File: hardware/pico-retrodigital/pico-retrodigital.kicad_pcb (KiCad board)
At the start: 2 copper layers, 53.8 x 35 mm, 23 parts, among them J1 Conn_02x05_Top_Bottom, J2 HDMI_A, J3 Conn_01x04, J6 Conn_01x02_Pin, U1 SN74LVC8T245, U2 SN74LVC8T245, U3 SN74LVC8T245, U4 74LVC2G17, U6 SN74LVC126A, U7 RP2350B

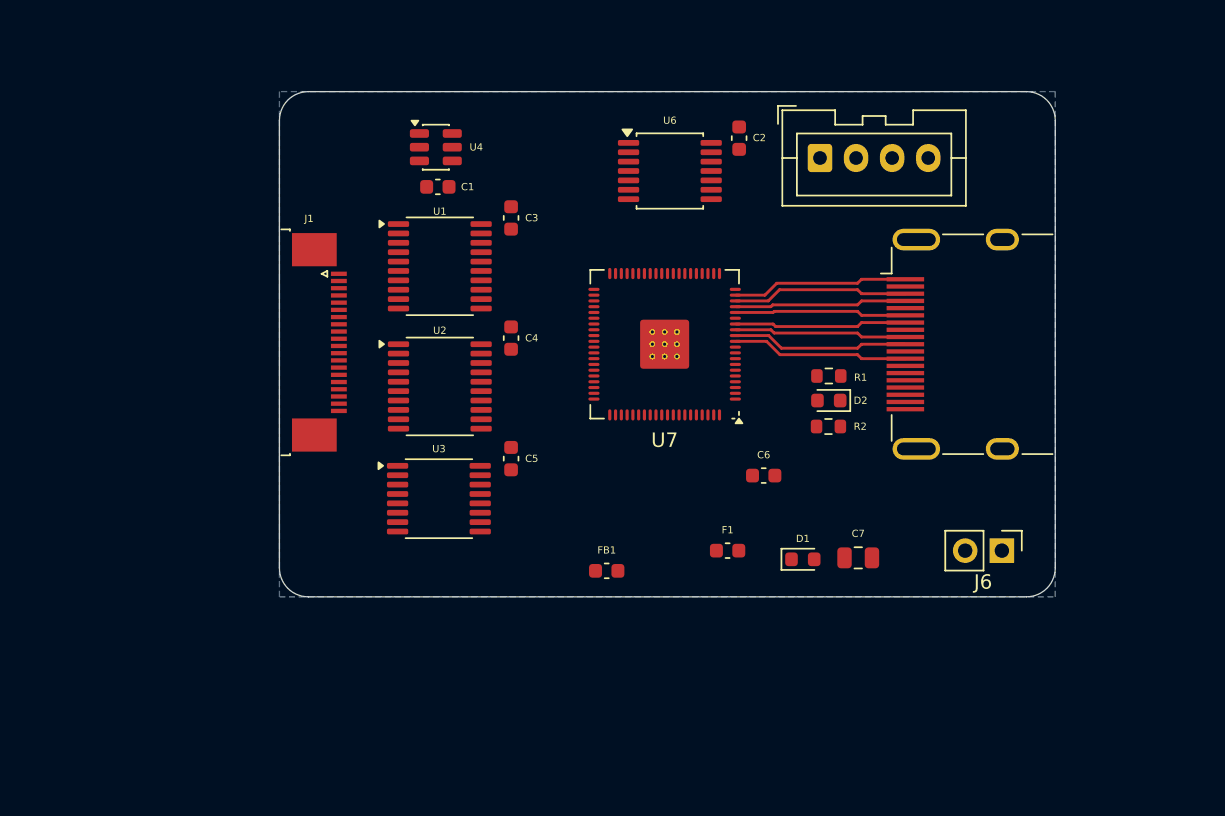
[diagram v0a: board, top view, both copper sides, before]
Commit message: Improve audio by adding 2s delay on startup
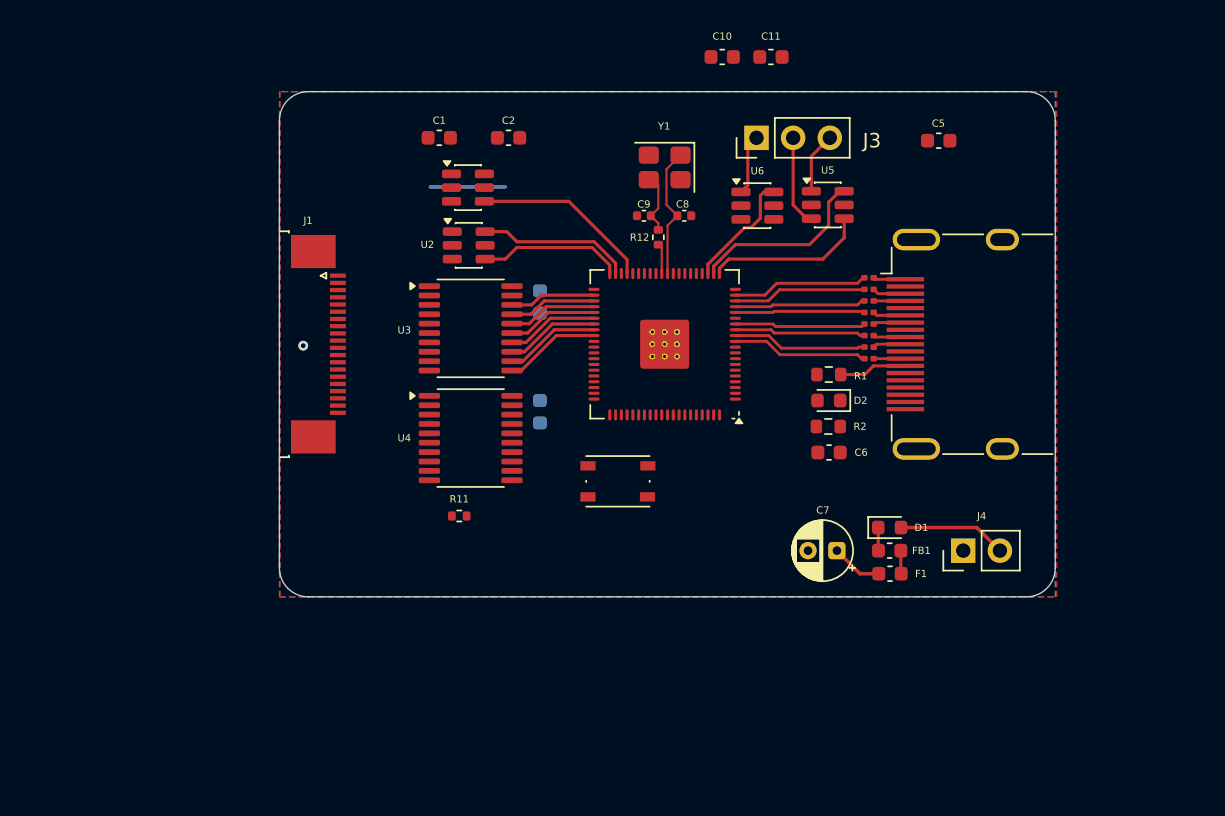
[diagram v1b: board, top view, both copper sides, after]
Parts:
- removed the C5 at (61.8, 100.4)
- removed J6: Conn_01x02_Pin, Connector_PinHeader_2.54mm:PinHeader_1x02_P2.54mm_Vertical
- removed the U3 at (56.8, 103.2)
- removed the U4 at (56.6, 78.8)
- added C10: 0.1u, Capacitor_SMD:C_0603_1608Metric, F.Cu at (76.4, 72.6)
- added C11: 0.1u, Capacitor_SMD:C_0603_1608Metric, F.Cu at (79.8, 72.6)
- added C2: 0.1u, Capacitor_SMD:C_0603_1608Metric, F.Cu at (61.6, 78.2)
- added C8: 15p, Capacitor_SMD:C_0402_1005Metric, F.Cu at (73.8, 83.6)
- added C9: 15p, Capacitor_SMD:C_0402_1005Metric, F.Cu at (71.0, 83.6)
- added J4: Conn_01x02_Pin, Connector_PinHeader_2.54mm:PinHeader_1x02_P2.54mm_Vertical, F.Cu at (93.1, 106.8)
- added R10: 220, Resistor_SMD:R_0201_0603Metric, F.Cu at (86.6, 87.9)
- added R11: 1k, Resistor_SMD:R_0402_1005Metric, F.Cu at (58.2, 104.4)
- added R12: 1k, Resistor_SMD:R_0402_1005Metric, F.Cu at (72.0, 85.1)
- added R3: 220, Resistor_SMD:R_0201_0603Metric, F.Cu at (86.6, 91.9)
- added R4: 220, Resistor_SMD:R_0201_0603Metric, F.Cu at (86.6, 93.5)
- added R5: 220, Resistor_SMD:R_0201_0603Metric, F.Cu at (86.6, 92.7)
- added R6: 220, Resistor_SMD:R_0201_0603Metric, F.Cu at (86.6, 91.1)
- added R7: 220, Resistor_SMD:R_0201_0603Metric, F.Cu at (86.6, 90.3)
- added R8: 220, Resistor_SMD:R_0201_0603Metric, F.Cu at (86.6, 89.5)
- added R9: 220, Resistor_SMD:R_0201_0603Metric, F.Cu at (86.6, 88.7)
- added SW1: SW_Push, Button_Switch_SMD:SW_Push_1P1T_NO_Vertical_Wuerth_434133025816, F.Cu at (69.2, 102.0)
- added U1: 74LVC2G17, Package_TO_SOT_SMD:SOT-23-6, F.Cu at (58.8, 81.7)
- added U2: 74LVC2G17, Package_TO_SOT_SMD:SOT-23-6, F.Cu at (58.9, 85.7)
- added U5: 74LVC2G17, Package_TO_SOT_SMD:SOT-23-6, F.Cu at (83.7, 82.8)
- added Y1: ABM8-272-T3, Crystal:Crystal_SMD_3225-4Pin_3.2x2.5mm, F.Cu at (72.4, 80.2)
- C3, C4: moved to B.Cu
- C7: footprint Capacitor_SMD:C_0805_2012Metric -> Capacitor_THT:CP_Radial_D4.0mm_P2.00mm
- J3: value Conn_01x04 -> Conn_01x03; footprint Connector_JST:JST_XA_B04B-XASK-1_1x04_P2.50mm_Vertical -> Connector_PinHeader_2.54mm:PinHeader_1x03_P2.54mm_Vertical
- U6: value SN74LVC126A -> 74LVC2G17; footprint Package_SO:TSSOP-14_4.4x5mm_P0.65mm -> Package_TO_SOT_SMD:SOT-23-6
- moved FB1 19.6 mm to (88.0, 106.8)
- moved C5 13.8 mm to (91.4, 78.4), turned to 0 degrees
- moved F1 11.4 mm to (88.0, 108.4), turned to 180 degrees
- moved U6 6.52 mm to (78.9, 82.9)
- moved D1 6.40 mm to (88.0, 105.2)
- moved C3 6.16 mm to (63.8, 89.6)
- moved C4 5.48 mm to (63.8, 97.2)
- moved U3 4.80 mm to (59.0, 91.4)
- moved C6 4.80 mm to (83.8, 100.0)
- moved J3 4.62 mm to (78.8, 78.2), turned to 90 degrees
- moved U4 4.17 mm to (59.0, 99.0)
- moved C1 3.40 mm to (56.8, 78.2), turned to 0 degrees
- moved C7 1.56 mm to (84.4, 106.8), turned to 180 degrees
- moved J1 0.15 mm to (48.5, 92.5)
- moved R1 0.10 mm to (83.8, 94.6)
- renumbered C2 to C5, U1 to U3, U2 to U4
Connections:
- C1 pad 1: +3V3 -> 3V3
- C3 pad 1: +3.3V -> 3V3
- C4 pad 1: +3.3V -> 3V3
- C7 pad 1: +5V -> 5V
- D1 pad 2: +5V MVS -> 5V
- D2 pad 2: +5V -> 5V
- F1 pad 2: +5V -> 5V
- J1 pad 1: IN_PCLK -> IN_VID_S
- J1 pad 10: IN_G1 -> IN_R4
- J1 pad 11: IN_G2 -> IN_G0
- J1 pad 12: IN_G3 -> IN_G1
- J1 pad 13: IN_G4 -> IN_G2
- J1 pad 14: IN_B0 -> IN_G3
- J1 pad 15: IN_B1 -> IN_G4
- J1 pad 16: IN_B2 -> IN_B0
- J1 pad 17: IN_B3 -> IN_B1
- J1 pad 18: IN_B4 -> IN_B2
- J1 pad 19: IN_VID_A -> IN_B3
- J1 pad 2: GND -> IN_PCLK
- J1 pad 20: IN_VID_B -> IN_B4
- J1 pad 3: IN_VID_C -> GND
- J1 pad 4: IN_R0 -> IN_VID_D1
- J1 pad 5: IN_R1 -> IN_VID_D2
- J1 pad 6: IN_R2 -> IN_R0
- J1 pad 7: IN_R3 -> IN_R1
- J1 pad 8: IN_R4 -> IN_R2
- J1 pad 9: IN_G0 -> IN_R3
- J3 pad 2: GND -> IN_AUD_B
- J3 pad 3: IN_AUD_B -> IN_AUD_A
- R1 pad 1: +3V3 -> 3V3
- R2 pad 1: +5V -> 5V
- U3 pad 20: +3.3V -> 3V3
- U4 pad 20: +3.3V -> 3V3
- U6 pad 1: unconnected-(U6-~{1OE}-Pad1) -> IN_AUD_C
- U6 pad 2: IN_AUD_A -> GND
- U6 pad 3: AUD_A -> unconnected-(U6-2A-Pad3)
- U6 pad 4: GND -> unconnected-(U6-2A-Pad4)
- U6 pad 5: IN_AUD_B -> 3V3
- U6 pad 6: AUD_B -> AUD_C
- U7 pad 11: CLK- -> Net-(U7-GPIO12)
- U7 pad 12: CLK+ -> Net-(U7-GPIO13)
- U7 pad 13: D0- -> Net-(U7-GPIO14)
- U7 pad 14: D0+ -> Net-(U7-GPIO15)
- U7 pad 16: D1- -> Net-(U7-GPIO16)
- U7 pad 17: D1+ -> Net-(U7-GPIO17)
- U7 pad 18: D2- -> Net-(U7-GPIO18)
- U7 pad 19: D2+ -> Net-(U7-GPIO19)
- U7 pad 21: unconnected-(U7-GPIO21-Pad21) -> AUD_A
- U7 pad 22: unconnected-(U7-GPIO22-Pad22) -> AUD_B
- U7 pad 23: unconnected-(U7-GPIO23-Pad23) -> AUD_C
- U7 pad 25: unconnected-(U7-GPIO24-Pad25) -> AUD_D
- U7 pad 28: unconnected-(U7-GPIO27-Pad28) -> VID_S
- U7 pad 30: unconnected-(U7-XIN-Pad30) -> XIN
- U7 pad 31: unconnected-(U7-XOUT-Pad31) -> XOUT
- U7 pad 37: unconnected-(U7-GPIO29-Pad37) -> PCLK
- U7 pad 39: unconnected-(U7-GPIO31-Pad39) -> VID_D1
- U7 pad 40: unconnected-(U7-GPIO32-Pad40) -> VID_D2
- U7 pad 42: unconnected-(U7-GPIO33-Pad42) -> R0
- U7 pad 43: unconnected-(U7-GPIO34-Pad43) -> R1
- U7 pad 44: unconnected-(U7-GPIO35-Pad44) -> R2
- U7 pad 45: unconnected-(U7-GPIO36-Pad45) -> R3
- U7 pad 46: unconnected-(U7-GPIO37-Pad46) -> R4
- U7 pad 47: unconnected-(U7-GPIO38-Pad47) -> G0
- U7 pad 48: unconnected-(U7-GPIO39-Pad48) -> G1
- U7 pad 49: unconnected-(U7-GPIO40_ADC0-Pad49) -> G2
- U7 pad 52: unconnected-(U7-GPIO41_ADC1-Pad52) -> G3
- U7 pad 53: unconnected-(U7-GPIO42_ADC2-Pad53) -> G4
- U7 pad 54: unconnected-(U7-GPIO43_ADC3-Pad54) -> B0
- U7 pad 55: unconnected-(U7-GPIO44_ADC4-Pad55) -> B1
- U7 pad 56: unconnected-(U7-GPIO45_ADC5-Pad56) -> B2
- U7 pad 57: unconnected-(U7-GPIO46_ADC6-Pad57) -> B3
- U7 pad 58: unconnected-(U7-GPIO47_ADC7-Pad58) -> B4
- U7 pad 62: Net-(U7-GND) -> GND
- U7 pad 75: unconnected-(U7-QSPI_SS-Pad75) -> Net-(U7-QSPI_SS)
- U7 pad 81: Net-(U7-GND) -> GND
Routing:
- net AUD_B: track 0.00 -> 12.6 mm
- net PCLK: track 0.00 -> 12.5 mm
- net AUD_A: track 0.00 -> 11.2 mm
- net 5V: track 0.00 -> 11.1 mm
- net VID_D1: track 0.00 -> 10.7 mm
- net VID_D2: track 0.00 -> 10.1 mm
- net CLK-: track 12.2 -> 2.19 mm
- net D2+: track 12.2 -> 2.24 mm
- net CLK+: track 12.2 -> 2.28 mm
- net D2-: track 12.2 -> 2.32 mm
- net D1+: track 11.9 -> 2.19 mm
- net D0-: track 11.9 -> 2.24 mm
- net D0+: track 11.9 -> 2.24 mm
- net D1-: track 11.9 -> 2.28 mm
- net Net-(U7-GPIO12): track 0.00 -> 9.44 mm
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- added copper zone on F.Cu, net GND

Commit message: PCB update
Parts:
- added C12: 10u, Capacitor_SMD:C_0805_2012Metric, F.Cu at (67.7, 122.4)
- added C5: 10u, Capacitor_SMD:C_0805_2012Metric, F.Cu at (83.3, 120.6)
- added J5: USB_C, Connector_USB:USB_Micro-B_Amphenol_10103594-0001LF_Horizontal, F.Cu at (91.8, 107.2)
- added R13: 27, Resistor_SMD:R_0402_1005Metric, F.Cu at (67.7, 116.4)
- added R14: 27, Resistor_SMD:R_0402_1005Metric, F.Cu at (74.0, 116.6)
- added U8: NCP1117-3.3_SOT223, Package_TO_SOT_SMD:SOT-223-3_TabPin2, F.Cu at (81.5, 104.7)
- moved C7 53.5 mm to (31.6, 115.6)
- moved D1 53.5 mm to (35.2, 114.0)
- moved FB1 53.5 mm to (35.2, 115.6)
- moved F1 53.5 mm to (35.2, 117.2)
- moved J4 53.5 mm to (40.3, 115.6)
- moved C6 24.2 mm to (106.4, 108.6)
- moved D2 24.2 mm to (106.4, 105.0)
- moved R2 24.2 mm to (106.4, 106.8)
- moved SW1 18.7 mm to (51.0, 106.4)
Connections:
- R11 pad 1: Net-(U7-QSPI_SS) -> Net-(R11-Pad1)
- R11 pad 2: Net-(R11-Pad2) -> Net-(U7-QSPI_SS)
- SW1 pad 2: Net-(R11-Pad2) -> Net-(R11-Pad1)
- U7 pad 66: unconnected-(U7-USB_DM-Pad66) -> Net-(U7-USB_DM)
- U7 pad 67: unconnected-(U7-USB_DP-Pad67) -> Net-(U7-USB_DP)

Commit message: Update PCB
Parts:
- added C13: 4.7u, Capacitor_SMD:C_0402_1005Metric, F.Cu at (70.4, 115.6)
- added R15: 33, Resistor_SMD:R_0402_1005Metric, F.Cu at (84.1, 113.6)
- C12, C5: footprint Capacitor_SMD:C_0805_2012Metric -> Capacitor_SMD:C_0402_1005Metric
- C4: moved to F.Cu
- moved C12 19.9 mm to (80.0, 106.8)
- moved J5 19.3 mm to (72.5, 107.2)
- moved R14 15.9 mm to (72.6, 101.3), turned to 90 degrees
- moved R13 15.5 mm to (71.6, 101.3), turned to 90 degrees
- moved C5 15.2 mm to (80.0, 105.8)
- moved C4 15.2 mm to (61.8, 112.2), turned to 0 degrees
- moved U8 4.88 mm to (86.3, 105.4), turned to 0 degrees
- moved R1 2.23 mm to (84.2, 96.8)
- renumbered R14 to R13, R13 to R14
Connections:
- C1 pad 1: 3V3 -> +3V3
- C10 pad 1: 3V3 -> +3V3
- C2 pad 1: 3V3 -> +3V3
- C3 pad 1: 3V3 -> +3V3
- C4 pad 1: 3V3 -> +3V3
- J5 pad 1: (no net) -> VBUS
- J5 pad 2: (no net) -> USB_D-
- J5 pad 3: (no net) -> USB_D+
- J5 pad 4: (no net) -> unconnected-(J5-ID-Pad4)
- J5 pad 5: (no net) -> GND
- J5 pad 6: (no net) -> GND
- R1 pad 1: 3V3 -> +3V3
- U1 pad 5: 3V3 -> +3V3
- U2 pad 5: 3V3 -> +3V3
- U3 pad 20: 3V3 -> +3V3
- U4 pad 20: 3V3 -> +3V3
- U5 pad 5: 3V3 -> +3V3
- U7 pad 61: unconnected-(U7-VREG_AVDD-Pad61) -> Net-(U7-VREG_AVDD)
- U7 pad 63: unconnected-(U7-VREG_LX-Pad63) -> Net-(U7-VREG_LX)
- U7 pad 64: unconnected-(U7-VREG_VIN-Pad64) -> +3V3
- U7 pad 65: unconnected-(U7-VREG_FB-Pad65) -> +1V1
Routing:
- net USB_D-: track 0.00 -> 3.73 mm
- net USB_D+: track 0.00 -> 3.72 mm
- net CEC_PICO: track 4.73 -> 5.79 mm
- removed copper zone on F.Cu, net GND

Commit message: Update hardware
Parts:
- removed C1, C2, C3: 0.1u, Capacitor_SMD:C_0603_1608Metric
- removed J3: Conn_01x03, Connector_PinHeader_2.54mm:PinHeader_1x03_P2.54mm_Vertical
- removed U1, U2, U5: 74LVC2G17, Package_TO_SOT_SMD:SOT-23-6
- removed U3, U4: SN74LVC8T245, Package_SO:TSSOP-20_4.4x6.5mm_P0.65mm
- J1: footprint Connector_FFC-FPC:TE_2-1734839-0_1x20-1MP_P0.5mm_Horizontal -> Connector_FFC-FPC:TE_3-1734839-2_1x32-1MP_P0.5mm_Horizontal
- moved U6 19.3 mm to (59.6, 84.2)
- moved SW1 2.38 mm to (53.3, 107.0)
- moved J1 1.10 mm to (49.5, 92.5)
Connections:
- J1 pad 1: IN_VID_S -> IN_PCLK
- J1 pad 10: IN_R4 -> R1
- J1 pad 11: IN_G0 -> R2
- J1 pad 12: IN_G1 -> R3
- J1 pad 13: IN_G2 -> R4
- J1 pad 14: IN_G3 -> G0
- J1 pad 15: IN_G4 -> G1
- J1 pad 16: IN_B0 -> G2
- J1 pad 17: IN_B1 -> G3
- J1 pad 18: IN_B2 -> G4
- J1 pad 19: IN_B3 -> B0
- J1 pad 2: IN_PCLK -> GND
- J1 pad 20: IN_B4 -> B1
- J1 pad 3: GND -> CMOD_0
- J1 pad 4: IN_VID_D1 -> CMOD_1
- J1 pad 5: IN_VID_D2 -> CMOD_2
- J1 pad 6: IN_R0 -> CMOD_3
- J1 pad 7: IN_R1 -> AUX_A
- J1 pad 8: IN_R2 -> AUX_B
- J1 pad 9: IN_R3 -> R0
- U6 pad 1: IN_AUD_C -> IN_AUD_CLK
- U6 pad 3: unconnected-(U6-2A-Pad3) -> IN_PCLK
- U6 pad 4: unconnected-(U6-2A-Pad4) -> PCLK
- U6 pad 6: AUD_C -> AUD_CLK
- U7 pad 21: AUD_A -> unconnected-(U7-GPIO21-Pad21)
- U7 pad 22: AUD_B -> CTL_0
- U7 pad 23: AUD_C -> CTL_1
- U7 pad 25: AUD_D -> CTL_2
- U7 pad 26: unconnected-(U7-GPIO25-Pad26) -> CTL_3
- U7 pad 27: unconnected-(U7-GPIO26-Pad27) -> CTL_4
- U7 pad 28: VID_S -> CTL_5
- U7 pad 36: unconnected-(U7-GPIO28-Pad36) -> PCLK
- U7 pad 37: PCLK -> CMOD_0
- U7 pad 38: unconnected-(U7-GPIO30-Pad38) -> CMOD_1
- U7 pad 39: VID_D1 -> CMOD_2
- U7 pad 40: VID_D2 -> CMOD_3
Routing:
- net G3: track 0.00 -> 16.8 mm
- net G4: track 0.00 -> 16.7 mm
- net B4: track 0.00 -> 16.7 mm
- net B0: track 0.00 -> 16.7 mm
- net B3: track 0.00 -> 16.7 mm
- net B2: track 0.00 -> 16.7 mm
- net B1: track 0.00 -> 16.7 mm
- net AUD_B: track 12.6 -> 0.00 mm
- net PCLK: track 12.5 -> 0.00 mm
- net AUD_A: track 11.2 -> 0.00 mm
- net R0: track 5.96 -> 16.8 mm
- net R1: track 6.06 -> 16.7 mm
- net VID_D1: track 10.7 -> 0.00 mm
- net R2: track 6.16 -> 16.7 mm
- net R3: track 6.27 -> 16.7 mm
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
